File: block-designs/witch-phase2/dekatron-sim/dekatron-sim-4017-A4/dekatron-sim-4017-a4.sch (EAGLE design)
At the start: 19 parts, among them IC1 4017D, IC2 74LVC1G125DBV

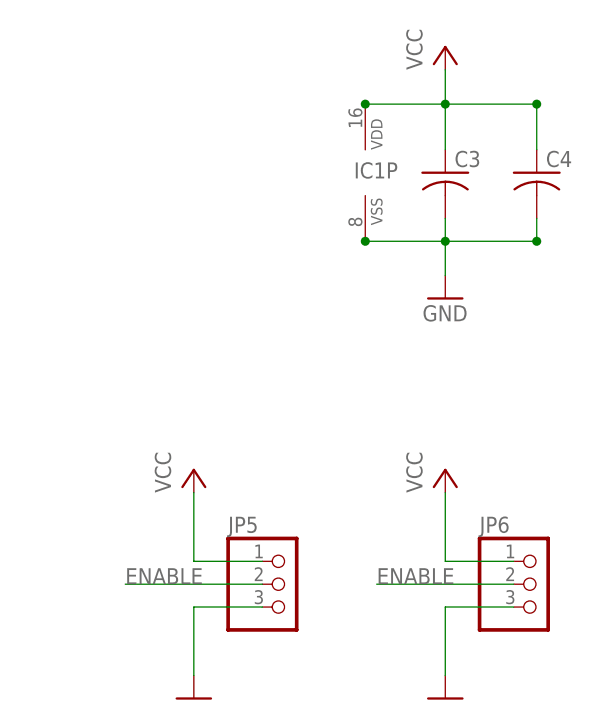
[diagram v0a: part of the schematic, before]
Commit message: updated designs for new labeling and spacing
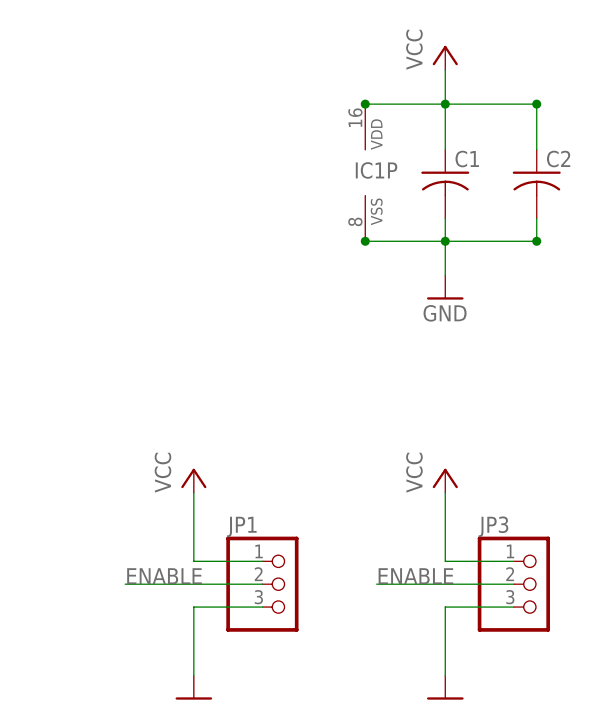
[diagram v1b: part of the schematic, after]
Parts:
- renumbered C3 to C1, C4 to C2, JP5 to JP1, JP6 to JP3
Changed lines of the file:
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@@
 <setting verticaltext="up"/>
 </settings>
-<grid distance="0.05" unitdist="inch" unit="inch" style="dots" multiple="1" display="no" altdistance="0.01" altunitdist="inch" altunit="inch"/>
+<grid distance="0.1" unitdist="inch" unit="inch" style="dots" multiple="1" display="no" altdistance="0.01" altunitdist="inch" altunit="inch"/>
 <layers>
 <layer number="1" name="Top" color="4" fill="1" visible="no" active="no"/>
@@
 <part name="LED9" library="led" deviceset="LED" device="CHIP-LED0805" value="RED"/>
 <part name="LED10" library="led" deviceset="LED" device="CHIP-LED0805" value="RED"/>
+<part name="GND3" library="supply1" deviceset="GND" device=""/>
+<part name="GND4" library="supply1" deviceset="GND" device=""/>
+<part name="GND6" library="supply1" deviceset="GND" device=""/>
+<part name="GND7" library="supply1" deviceset="GND" device=""/>
 <part name="GND5" library="supply1" deviceset="GND" device=""/>
-<part name="GND6" library="supply1" deviceset="GND" device=""/>
-<part name="GND8" library="supply1" deviceset="GND" device=""/>
-<part name="GND9" library="supply1" deviceset="GND" device=""/>
-<part name="GND7" library="supply1" deviceset="GND" device=""/>
-<part name="C3" library="resistor" deviceset="C-US" device="C0805"/>
-<part name="C4" library="resistor" deviceset="C-US" device="C0805"/>
+<part name="C1" library="resistor" deviceset="C-US" device="C0805"/>
+<part name="C2" library="resistor" deviceset="C-US" device="C0805"/>
 <part name="FRAME1" library="frames" deviceset="LETTER_L" device=""/>
 <part name="IC2" library="74xx-little-us" deviceset="74*1G125" device="DBV" technology="LVC" value="74LVC1G125DBV"/>
 <part name="JP2" library="pinhead" deviceset="PINHD-1X4" device=""/>
 <part name="JP4" library="pinhead" deviceset="PINHD-1X4" device=""/>
-<part name="GND4" library="supply1" deviceset="GND" device=""/>
+<part name="GND2" library="supply1" deviceset="GND" device=""/>
 <part name="GND1" library="supply1" deviceset="GND" device=""/>
 <part name="R1" library="resistor" deviceset="R-US_" device="R0805"/>
-<part name="JP5" library="pinhead" deviceset="PINHD-1X3" device=""/>
-<part name="JP6" library="pinhead" deviceset="PINHD-1X3" device=""/>
+<part name="JP1" library="pinhead" deviceset="PINHD-1X3" device=""/>
+<part name="JP3" library="pinhead" deviceset="PINHD-1X3" device=""/>
+<part name="P+3" library="supply1" deviceset="VCC" device=""/>
 <part name="P+1" library="supply1" deviceset="VCC" device=""/>
+<part name="P+4" library="supply1" deviceset="VCC" device=""/>
 <part name="P+2" library="supply1" deviceset="VCC" device=""/>
-<part name="P+3" library="supply1" deviceset="VCC" device=""/>
-<part name="P+4" library="supply1" deviceset="VCC" device=""/>
 <part name="P+5" library="supply1" deviceset="VCC" device=""/>
 </parts>
@@
 <attribute name="NAME" x="25.908" y="39.624" size="1.778" layer="95"/>
 </instance>
-<instance part="GND5" gate="1" x="190.5" y="109.22"/>
-<instance part="GND6" gate="1" x="190.5" y="71.12"/>
-<instance part="GND8" gate="1" x="218.44" y="109.22"/>
-<instance part="GND9" gate="1" x="218.44" y="71.12"/>
-<instance part="GND7" gate="1" x="218.44" y="153.67"/>
-<instance part="C3" gate="G$1" x="218.44" y="167.64"/>
-<instance part="C4" gate="G$1" x="228.6" y="167.64"/>
+<instance part="GND3" gate="1" x="190.5" y="109.22"/>
+<instance part="GND4" gate="1" x="190.5" y="71.12"/>
+<instance part="GND6" gate="1" x="218.44" y="109.22"/>
+<instance part="GND7" gate="1" x="218.44" y="71.12"/>
+<instance part="GND5" gate="1" x="218.44" y="153.67"/>
+<instance part="C1" gate="G$1" x="218.44" y="167.64"/>
+<instance part="C2" gate="G$1" x="228.6" y="167.64"/>
 <instance part="FRAME1" gate="G$1" x="0" y="0"/>
 <instance part="FRAME1" gate="G$2" x="147.32" y="0"/>
@@
 <instance part="JP2" gate="A" x="200.66" y="83.82"/>
 <instance part="JP4" gate="A" x="228.6" y="83.82"/>
-<instance part="GND4" gate="1" x="144.78" y="116.84"/>
+<instance part="GND2" gate="1" x="144.78" y="116.84"/>
 <instance part="GND1" gate="1" x="7.62" y="12.7"/>
 <instance part="R1" gate="G$1" x="7.62" y="27.94" rot="R90"/>
-<instance part="JP5" gate="A" x="200.66" y="121.92"/>
-<instance part="JP6" gate="A" x="228.6" y="121.92"/>
-<instance part="P+1" gate="VCC" x="218.44" y="181.61"/>
-<instance part="P+2" gate="VCC" x="190.5" y="134.62"/>
-<instance part="P+3" gate="VCC" x="218.44" y="134.62"/>
-<instance part="P+4" gate="VCC" x="190.5" y="99.06"/>
+<instance part="JP1" gate="A" x="200.66" y="121.92"/>
+<instance part="JP3" gate="A" x="228.6" y="121.92"/>
+<instance part="P+3" gate="VCC" x="218.44" y="181.61"/>
+<instance part="P+1" gate="VCC" x="190.5" y="134.62"/>
+<instance part="P+4" gate="VCC" x="218.44" y="134.62"/>
+<instance part="P+2" gate="VCC" x="190.5" y="99.06"/>
 <instance part="P+5" gate="VCC" x="218.44" y="99.06"/>
 <instance part="IC1" gate="P" x="209.55" y="167.64"/>
@@
 <wire x1="198.12" y1="119.38" x2="190.5" y2="119.38" width="0.1524" layer="91"/>
 <wire x1="190.5" y1="119.38" x2="190.5" y2="111.76" width="0.1524" layer="91"/>
-<pinref part="GND5" gate="1" pin="GND"/>
-<pinref part="JP5" gate="A" pin="3"/>
+<pinref part="GND3" gate="1" pin="GND"/>
+<pinref part="JP1" gate="A" pin="3"/>
 </segment>
 <segment>
 <wire x1="190.5" y1="81.28" x2="190.5" y2="73.66" width="0.1524" layer="91"/>
-<pinref part="GND6" gate="1" pin="GND"/>
+<pinref part="GND4" gate="1" pin="GND"/>
 <wire x1="190.5" y1="81.28" x2="198.12" y2="81.28" width="0.1524" layer="91"/>
 <pinref part="JP2" gate="A" pin="4"/>
@@
 <wire x1="226.06" y1="119.38" x2="218.44" y2="119.38" width="0.1524" layer="91"/>
 <wire x1="218.44" y1="119.38" x2="218.44" y2="111.76" width="0.1524" layer="91"/>
-<pinref part="GND8" gate="1" pin="GND"/>
-<pinref part="JP6" gate="A" pin="3"/>
+<pinref part="GND6" gate="1" pin="GND"/>
+<pinref part="JP3" gate="A" pin="3"/>
 </segment>
 <segment>
 <wire x1="218.44" y1="81.28" x2="218.44" y2="73.66" width="0.1524" layer="91"/>
-<pinref part="GND9" gate="1" pin="GND"/>
+<pinref part="GND7" gate="1" pin="GND"/>
 <wire x1="218.44" y1="81.28" x2="226.06" y2="81.28" width="0.1524" layer="91"/>
 <pinref part="JP4" gate="A" pin="4"/>
 </segment>
 <segment>
-<pinref part="C3" gate="G$1" pin="2"/>
+<pinref part="C1" gate="G$1" pin="2"/>
 <wire x1="218.44" y1="162.56" x2="218.44" y2="160.02" width="0.1524" layer="91"/>
-<pinref part="C4" gate="G$1" pin="2"/>
+<pinref part="C2" gate="G$1" pin="2"/>
 <wire x1="228.6" y1="162.56" x2="228.6" y2="160.02" width="0.1524" layer="91"/>
 <wire x1="228.6" y1="160.02" x2="218.44" y2="160.02" width="0.1524" layer="91"/>
 <junction x="228.6" y="160.02"/>
 <junction x="218.44" y="160.02"/>
-<pinref part="GND7" gate="1" pin="GND"/>
+<pinref part="GND5" gate="1" pin="GND"/>
 <wire x1="218.44" y1="156.21" x2="218.44" y2="160.02" width="0.1524" layer="91"/>
 <pinref part="IC1" gate="P" pin="VSS"/>
@@
 <wire x1="139.7" y1="127" x2="144.78" y2="127" width="0.1524" layer="91"/>
 <wire x1="144.78" y1="127" x2="144.78" y2="119.38" width="0.1524" layer="91"/>
-<pinref part="GND4" gate="1" pin="GND"/>
+<pinref part="GND2" gate="1" pin="GND"/>
 </segment>
 <segment>
@@
 <wire x1="198.12" y1="121.92" x2="182.88" y2="121.92" width="0.1524" layer="91"/>
 <label x="182.88" y="121.92" size="1.778" layer="95"/>
-<pinref part="JP5" gate="A" pin="2"/>
+<pinref part="JP1" gate="A" pin="2"/>
 </segment>
 <segment>
 <wire x1="226.06" y1="121.92" x2="210.82" y2="121.92" width="0.1524" layer="91"/>
 <label x="210.82" y="121.92" size="1.778" layer="95"/>
-<pinref part="JP6" gate="A" pin="2"/>
+<pinref part="JP3" gate="A" pin="2"/>
 </segment>
 <segment>
@@
 <net name="VCC" class="0">
 <segment>
-<pinref part="C3" gate="G$1" pin="1"/>
+<pinref part="C1" gate="G$1" pin="1"/>
 <wire x1="218.44" y1="175.26" x2="218.44" y2="170.18" width="0.1524" layer="91"/>
-<pinref part="C4" gate="G$1" pin="1"/>
+<pinref part="C2" gate="G$1" pin="1"/>
 <wire x1="218.44" y1="175.26" x2="228.6" y2="175.26" width="0.1524" layer="91"/>
 <wire x1="228.6" y1="175.26" x2="228.6" y2="170.18" width="0.1524" layer="91"/>
@@
 <junction x="228.6" y="175.26"/>
 <wire x1="218.44" y1="175.26" x2="218.44" y2="179.07" width="0.1524" layer="91"/>
-<pinref part="P+1" gate="VCC" pin="VCC"/>
+<pinref part="P+3" gate="VCC" pin="VCC"/>
 <pinref part="IC1" gate="P" pin="VDD"/>
 <wire x1="218.44" y1="175.26" x2="209.55" y2="175.26" width="0.1524" layer="91"/>
@@
 <wire x1="198.12" y1="124.46" x2="190.5" y2="124.46" width="0.1524" layer="91"/>
 <wire x1="190.5" y1="124.46" x2="190.5" y2="132.08" width="0.1524" layer="91"/>
-<pinref part="JP5" gate="A" pin="1"/>
-<pinref part="P+2" gate="VCC" pin="VCC"/>
+<pinref part="JP1" gate="A" pin="1"/>
+<pinref part="P+1" gate="VCC" pin="VCC"/>
 </segment>
 <segment>
 <wire x1="226.06" y1="124.46" x2="218.44" y2="124.46" width="0.1524" layer="91"/>
 <wire x1="218.44" y1="124.46" x2="218.44" y2="132.08" width="0.1524" layer="91"/>
-<pinref part="JP6" gate="A" pin="1"/>
-<pinref part="P+3" gate="VCC" pin="VCC"/>
+<pinref part="JP3" gate="A" pin="1"/>
+<pinref part="P+4" gate="VCC" pin="VCC"/>
 </segment>
 <segment>
@@
 <wire x1="190.5" y1="88.9" x2="190.5" y2="96.52" width="0.1524" layer="91"/>
 <pinref part="JP2" gate="A" pin="1"/>
-<pinref part="P+4" gate="VCC" pin="VCC"/>
-</segment>
-<segment>
+<pinref part="P+2" gate="VCC" pin="VCC"/>
+</segment>
+<segment>

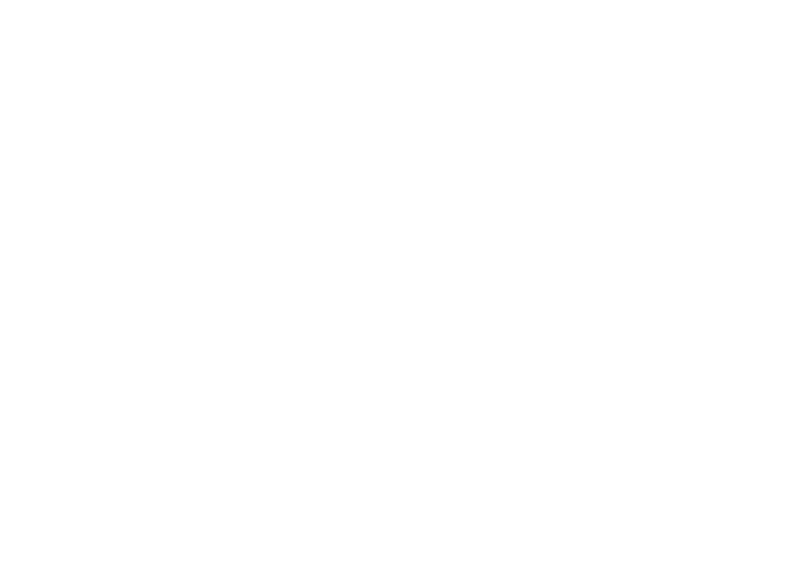
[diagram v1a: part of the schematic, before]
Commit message: add fiducials for pick-and-place
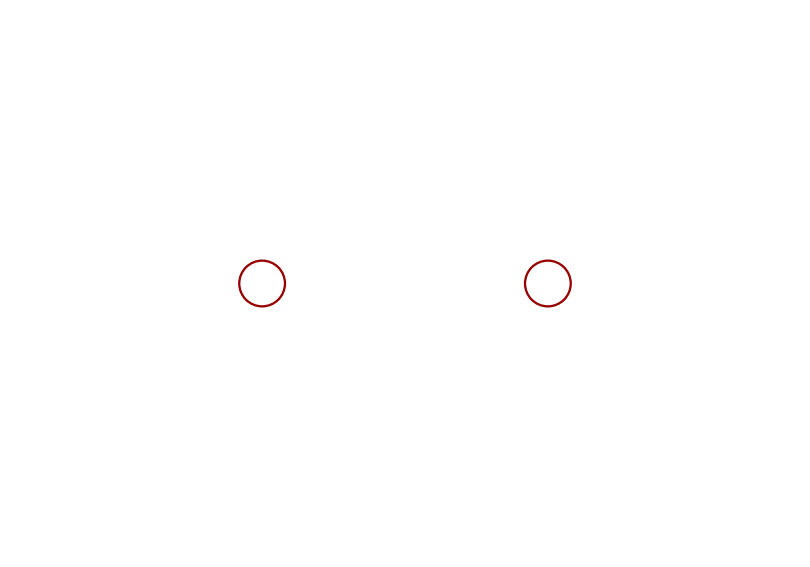
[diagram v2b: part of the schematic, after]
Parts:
- added FID1, FID2: FIDUCIAL, adafruit:FIDUCIAL
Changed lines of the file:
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@@
 <?xml version="1.0" encoding="utf-8"?>
 <!DOCTYPE eagle SYSTEM "eagle.dtd">
-<eagle version="7.3.0">
+<eagle version="7.6.0">
 <drawing>
 <settings>
@@
 <setting verticaltext="up"/>
 </settings>
-<grid distance="0.1" unitdist="inch" unit="inch" style="dots" multiple="1" display="no" altdistance="0.01" altunitdist="inch" altunit="inch"/>
+<grid distance="0.05" unitdist="inch" unit="inch" style="dots" multiple="1" display="no" altdistance="0.01" altunitdist="inch" altunit="inch"/>
 <layers>
 <layer number="1" name="Top" color="4" fill="1" visible="no" active="no"/>
@@
 <layer number="54" name="bGND_GNDA" color="1" fill="9" visible="no" active="no"/>
 <layer number="56" name="wert" color="7" fill="1" visible="no" active="no"/>
+<layer number="57" name="tCAD" color="7" fill="1" visible="no" active="no"/>
+<layer number="59" name="tCarbon" color="7" fill="1" visible="no" active="no"/>
+<layer number="60" name="bCarbon" color="7" fill="1" visible="no" active="no"/>
+<layer number="90" name="Modules" color="5" fill="1" visible="yes" active="yes"/>
 <layer number="91" name="Nets" color="2" fill="1" visible="yes" active="yes"/>
 <layer number="92" name="Busses" color="1" fill="1" visible="yes" active="yes"/>
@@
 <layer number="106" name="bPlate" color="7" fill="1" visible="yes" active="yes"/>
 <layer number="107" name="Crop" color="7" fill="1" visible="yes" active="yes"/>
+<layer number="108" name="tplace-old" color="10" fill="1" visible="yes" active="yes"/>
+<layer number="109" name="ref-old" color="11" fill="1" visible="yes" active="yes"/>
+<layer number="110" name="fp0" color="7" fill="1" visible="yes" active="yes"/>
+<layer number="111" name="LPC17xx" color="7" fill="1" visible="yes" active="yes"/>
+<layer number="112" name="tSilk" color="7" fill="1" visible="yes" active="yes"/>
+<layer number="113" name="IDFDebug" color="7" fill="1" visible="yes" active="yes"/>
 <layer number="116" name="Patch_BOT" color="9" fill="4" visible="yes" active="yes"/>
+<layer number="118" name="Rect_Pads" color="7" fill="1" visible="yes" active="yes"/>
 <layer number="121" name="_tsilk" color="7" fill="1" visible="yes" active="yes"/>
 <layer number="122" name="_bsilk" color="7" fill="1" visible="yes" active="yes"/>
+<layer number="123" name="tTestmark" color="7" fill="1" visible="yes" active="yes"/>
+<layer number="124" name="bTestmark" color="7" fill="1" visible="yes" active="yes"/>
 <layer number="125" name="_tNames" color="7" fill="1" visible="yes" active="yes"/>
+<layer number="126" name="_bNames" color="7" fill="1" visible="yes" active="yes"/>
+<layer number="127" name="_tValues" color="7" fill="1" visible="yes" active="yes"/>
+<layer number="128" name="_bValues" color="7" fill="1" visible="yes" active="yes"/>
+<layer number="129" name="Mask" color="7" fill="1" visible="no" active="yes"/>
+<layer number="131" name="tAdjust" color="7" fill="1" visible="yes" active="yes"/>
+<layer number="132" name="bAdjust" color="7" fill="1" visible="yes" active="yes"/>
 <layer number="144" name="Drill_legend" color="7" fill="1" visible="yes" active="yes"/>
+<layer number="145" name="DrillLegend_01-16" color="2" fill="9" visible="yes" active="yes"/>
+<layer number="150" name="Notes" color="7" fill="1" visible="yes" active="yes"/>
 <layer number="151" name="HeatSink" color="7" fill="1" visible="yes" active="yes"/>
+<layer number="152" name="_bDocu" color="7" fill="1" visible="yes" active="yes"/>
+<layer number="153" name="FabDoc1" color="7" fill="1" visible="yes" active="yes"/>
+<layer number="154" name="FabDoc2" color="7" fill="1" visible="yes" active="yes"/>
+<layer number="155" name="FabDoc3" color="7" fill="1" visible="yes" active="yes"/>
+<layer number="199" name="Contour" color="7" fill="1" visible="yes" active="yes"/>
 <layer number="200" name="200bmp" color="1" fill="10" visible="yes" active="yes"/>
 <layer number="201" name="201bmp" color="2" fill="10" visible="yes" active="yes"/>
@@
 <layer number="223" name="223bmp" color="24" fill="1" visible="no" active="no"/>
 <layer number="224" name="224bmp" color="25" fill="1" visible="no" active="no"/>
+<layer number="225" name="225bmp" color="7" fill="1" visible="no" active="yes"/>
+<layer number="226" name="226bmp" color="7" fill="1" visible="no" active="yes"/>
+<layer number="227" name="227bmp" color="7" fill="1" visible="no" active="yes"/>
+<layer number="228" name="228bmp" color="7" fill="1" visible="no" active="yes"/>
+<layer number="229" name="229bmp" color="7" fill="1" visible="no" active="yes"/>
+<layer number="230" name="230bmp" color="7" fill="1" visible="no" active="yes"/>
+<layer number="231" name="231bmp" color="7" fill="1" visible="no" active="yes"/>
+<layer number="232" name="Eagle3D_PG2" color="7" fill="1" visible="no" active="no"/>
+<layer number="233" name="Eagle3D_PG3" color="7" fill="1" visible="no" active="no"/>
+<layer number="248" name="Housing" color="7" fill="1" visible="yes" active="yes"/>
+<layer number="249" name="Edge" color="7" fill="1" visible="yes" active="yes"/>
 <layer number="250" name="Descript" color="3" fill="1" visible="no" active="no"/>
 <layer number="251" name="SMDround" color="12" fill="11" visible="no" active="no"/>
 <layer number="254" name="cooling" color="7" fill="1" visible="yes" active="yes"/>
+<layer number="255" name="routoute" color="7" fill="1" visible="yes" active="yes"/>
 </layers>
 <schematic xreflabel="%F%N/%S.%C%R" xrefpart="/%S.%C%R">
@@
 <part name="P+2" library="supply1" deviceset="VCC" device=""/>
 <part name="P+5" library="supply1" deviceset="VCC" device=""/>
+<part name="FID1" library="adafruit" deviceset="FIDUCIAL" device=""/>
+<part name="FID2" library="adafruit" deviceset="FIDUCIAL" device=""/>
 </parts>
 <sheets>
@@
 <instance part="P+5" gate="VCC" x="218.44" y="99.06"/>
 <instance part="IC1" gate="P" x="209.55" y="167.64"/>
+<instance part="FID1" gate="G$1" x="110.49" y="53.34"/>
+<instance part="FID2" gate="G$1" x="142.24" y="53.34"/>
 </instances>
 <busses>
